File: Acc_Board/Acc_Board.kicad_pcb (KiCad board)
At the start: 2 copper layers, 139.7 x 88.9 mm, 85 parts, among them J1 AIRs Power, J10 Conn_01x02_Pin, J12 776087-1, J2 IsoSPI, J3 IMD BAT, J4 HV Power, J5 HVIL, J6 IMD, J7 Current Sensor, J8 Fans, J9 Shutdown IL, K1 Relay_SPST-NO, K2 Latching Relay, Q1 STS6NF20V, Q2 STS6NF20V, Q3 STS6NF20V, Q4 STS6NF20V, U1 ISO1050DUB, U10 DK1A1B-12V, U11 NSL-32, U12 LTC6820, U13 NAND, U15 MCP6004, U16 NSL-32, U17 NSL-32, U2 NUCLEO-L432KC, U3 LM555N, U4 PQDE6W-Q110-S5-H-D, U5 R-78B5.0-2.0, U6 NSL-32, U7 DK1A1B-12V, U8 LM7809_TO220, U9 NSL-32

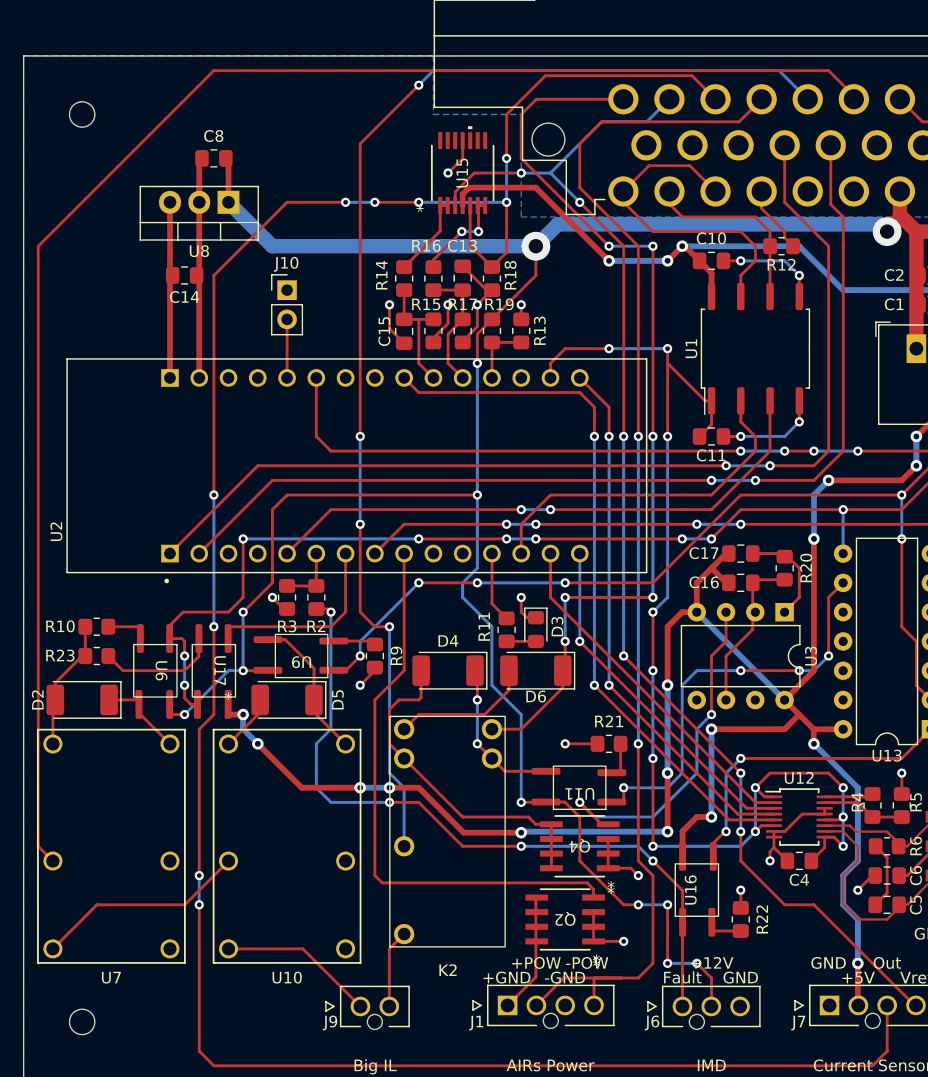
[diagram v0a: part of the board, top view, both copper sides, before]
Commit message: acc board fixed opto footprints
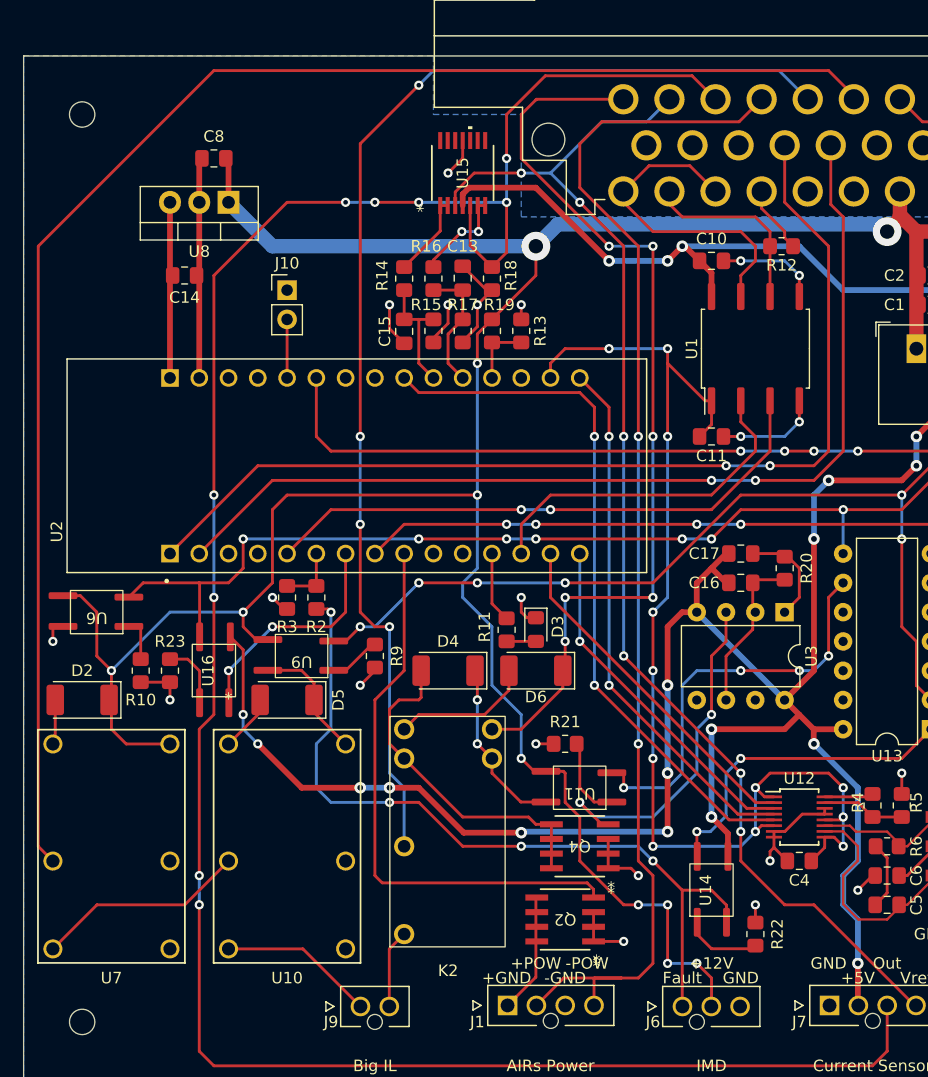
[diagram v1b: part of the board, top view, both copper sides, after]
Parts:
- removed U17: NSL-32, 1FS_2_Global_Footprint_Library:OptoCoupler 6-SOP
- added U14: TLP3122AE, 1FS_2_Global_Footprint_Library:OptoCoupler 6-SOP, F.Cu at (72.4, 85.1)
- U11, U16, U6, U9: value NSL-32 -> TLP3122AE
- moved U16 46.0 mm to (29.2, 66.0)
- moved U6 7.18 mm to (19.1, 61.0), turned to 180 degrees
- moved R23 6.48 mm to (25.4, 66.0), turned to -90 degrees
- moved R10 5.39 mm to (22.9, 66.0), turned to -90 degrees
- moved R21 3.81 mm to (59.7, 72.4)
- moved R22 1.80 mm to (76.2, 88.9)
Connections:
- D2 pad 1: Net-(D2-K) -> +12V
- R10 pad 1: Net-(U6-K) -> Net-(R10-Pad1)
- R21 pad 1: Net-(U11-K) -> Net-(R21-Pad1)
- R22 pad 1: Net-(U16-K) -> Net-(R22-Pad1)
- R23 pad 1: Net-(U17-K) -> Net-(R23-Pad1)
- R9 pad 2: Net-(U9-K) -> Net-(R9-Pad2)
- U11 pad 1: Net-(U11-A) -> Net-(R21-Pad1)
- U11 pad 3: Net-(D4-K) -> Net-(U11-Pad3)
- U13 pad 9: Net-(U11-A) -> Net-(U11-Pad3)
- U16 pad 1: /IMD_FAULT -> Net-(R23-Pad1)
- U16 pad 3: /IMD_FAULT_5V -> /BMS_FAULT
- U6 pad 1: /BMS_FAULT_5V -> Net-(R10-Pad1)
- U6 pad 3: Net-(D2-K) -> /BMS_FAULT_5V
- U7 pad 8: Net-(D2-K) -> +12V
- U9 pad 1: /IMD_FAULT_5V -> Net-(R9-Pad2)
- U9 pad 3: Net-(D5-K) -> /IMD_FAULT_5V
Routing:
- net Net-(U11-A): track 36.0 -> 0.00 mm, vias 4 -> 0
- net Net-(U11-Pad3): track 0.00 -> 35.1 mm, vias 0 -> 4
- net +12V: track 289.0 -> 310.5 mm, vias 12 -> 11
- net Net-(U17-K): track 10.4 -> 0.00 mm
- net Net-(D2-K): track 7.75 -> 0.00 mm
- net Net-(R21-Pad1): track 0.00 -> 7.22 mm
- net Net-(R22-Pad1): track 0.00 -> 6.73 mm
- net /IMD_FAULT: track 62.7 -> 68.5 mm
- net Net-(R23-Pad1): track 0.00 -> 5.75 mm
- net Net-(R9-Pad2): track 0.00 -> 4.49 mm
- net +5V: track 244.3 -> 248.1 mm
- net Net-(U9-K): track 3.69 -> 0.00 mm
- net /BMS_FAULT: track 16.8 -> 20.1 mm, vias 0 -> 2
- net Net-(U11-K): track 3.13 -> 0.00 mm
- net Net-(U16-K): track 3.13 -> 0.00 mm
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
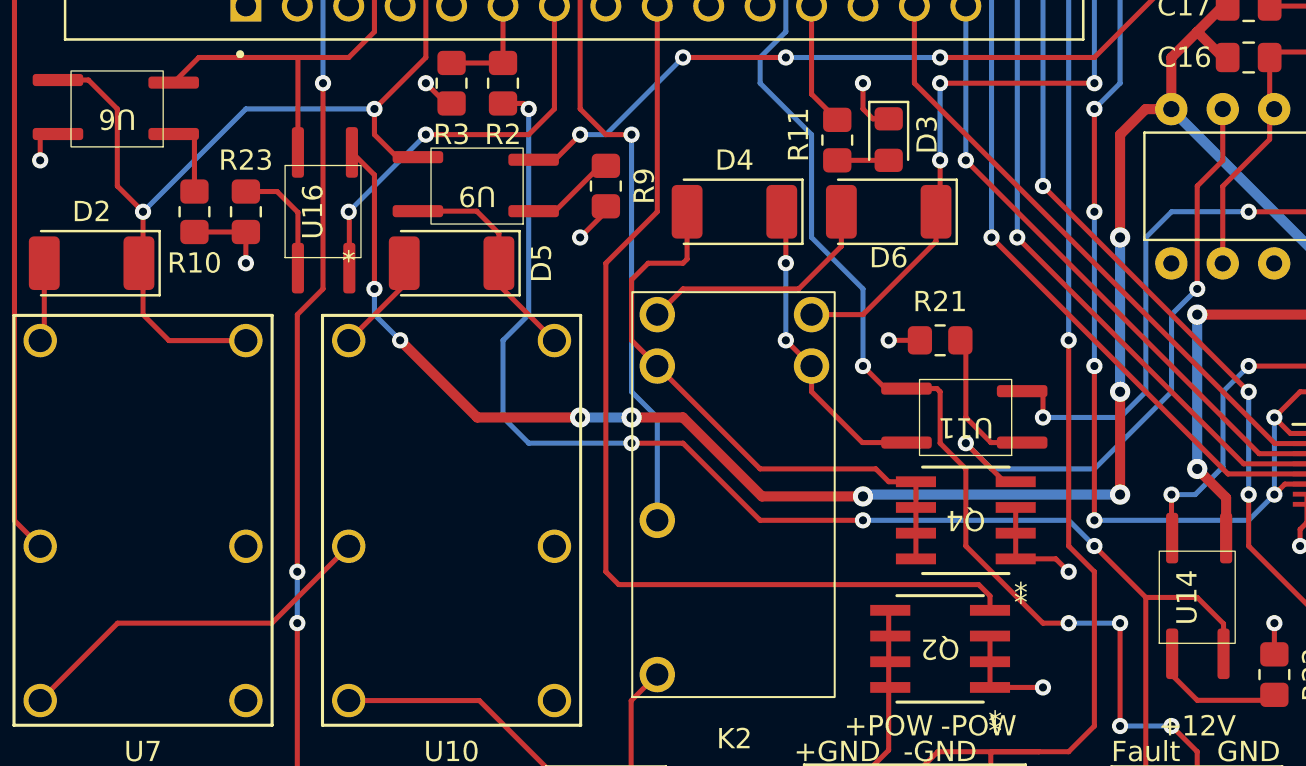
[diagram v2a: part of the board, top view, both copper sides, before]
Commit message: fixed opto silkscreen on acc board
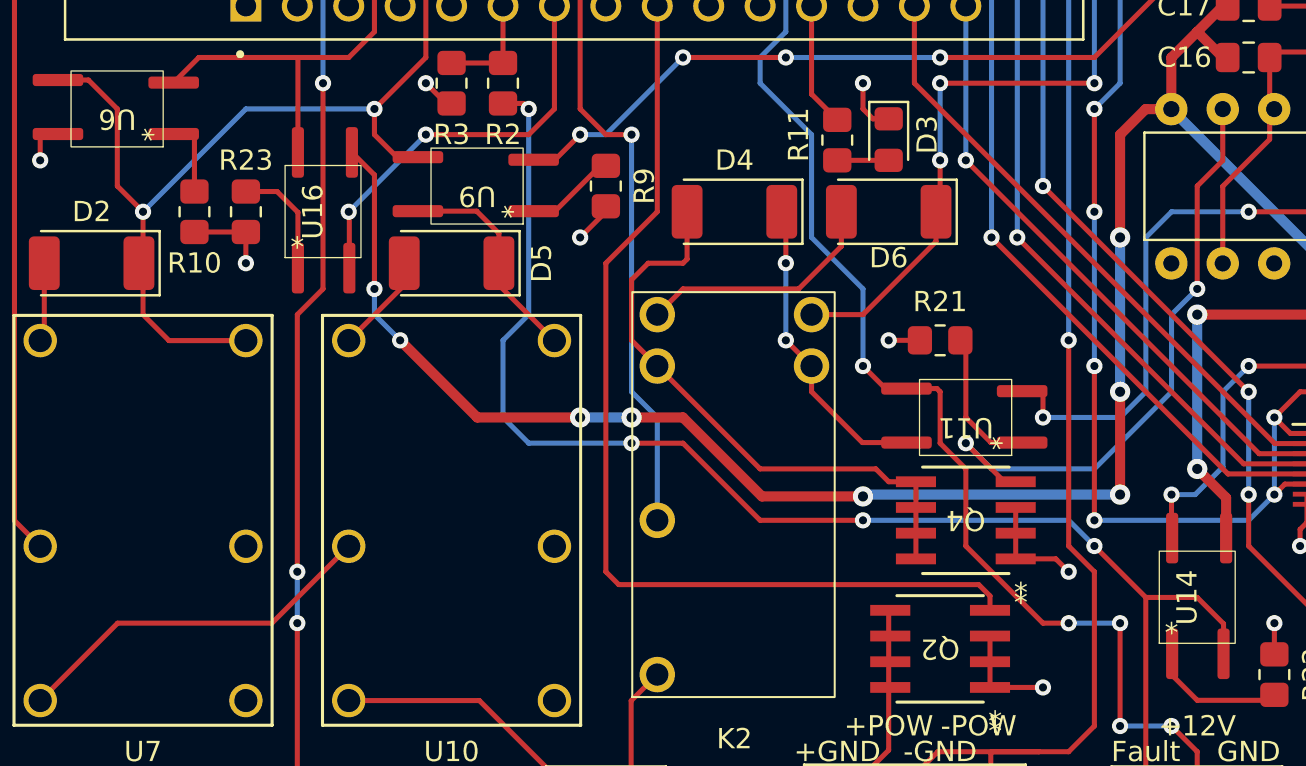
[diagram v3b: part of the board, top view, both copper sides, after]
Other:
- board text added: "*"
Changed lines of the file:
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@@
         (effects (font (size 1 1) (thickness 0.15)))
     )
-    (fp_text user "*" (at 0 -3.928533 unlocked) (layer "F.SilkS")
-        (effects (font (size 1 1) (thickness 0.15)))
-    )
     (fp_text user "*" (at 0 -1.693333 unlocked) (layer "F.Fab")
         (effects (font (size 1 1) (thickness 0.15)))
@@
     (effects (font (size 1 1) (thickness 0.15)) (justify right mirror))
   )
+  (gr_text "*" (at 71.12 86.36 180) (layer "F.SilkS")
+    (effects (font (size 1 1) (thickness 0.15)))
+  )
   (gr_text "L" (at 142.24 35.56 90) (layer "F.SilkS")
     (effects (font (size 1 1) (thickness 0.15)))
@@
     (effects (font (size 1 1) (thickness 0.15)))
   )
+  (gr_text "*" (at 38.1 66.04 -90) (layer "F.SilkS")
+    (effects (font (size 1 1) (thickness 0.15)))
+  )
   (gr_text "N" (at 143.51 80.01 90) (layer "F.SilkS")
     (effects (font (size 1 1) (thickness 0.15)))
@@
     (effects (font (size 1 1) (thickness 0.15)))
   )
+  (gr_text "*" (at 27.94 67.31 180) (layer "F.SilkS")
+    (effects (font (size 1 1) (thickness 0.15)))
+  )
   (gr_text "TS-" (at 109.855 92.71) (layer "F.SilkS")
     (effects (font (size 1 1) (thickness 0.15)))
@@
     (effects (font (size 1 1) (thickness 0.15)))
   )
+  (gr_text "*" (at 62.23 77.47 -90) (layer "F.SilkS")
+    (effects (font (size 1 1) (thickness 0.15)))
+  )
   (gr_text "TS" (at 105.41 88.9) (layer "F.SilkS")
     (effects (font (size 1 1) (thickness 0.15)) (justify left))
@@
     (effects (font (size 1 1) (thickness 0.15)))
   )
+  (gr_text "*" (at 20.32 62.23 -90) (layer "F.SilkS")
+    (effects (font (size 1 1) (thickness 0.15)))
+  )

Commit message: Updade acc board version #
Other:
- board text added: "FS-2 Acc Board Formula Slug V 1.5"
- board text removed: "FS-2 Acc Board Formula Slug V 1.4"
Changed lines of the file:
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@@
   (title_block
     (title "Accumulator Board")
-    (date "2024-02-26")
-    (rev "1.4")
+    (date "2024-03-01")
+    (rev "1.5")
     (company "Formula Slug")
   )
@@
     (effects (font (size 1 1) (thickness 0.15)))
   )
-  (gr_text "FS-2 Acc Board\nFormula Slug\nV 1.4" (at 124.46 33.02) (layer "F.SilkS")
+  (gr_text "FS-2 Acc Board\nFormula Slug\nV 1.5" (at 124.46 33.02) (layer "F.SilkS")
     (effects (font (size 1 1) (thickness 0.15)) (justify left))
   )

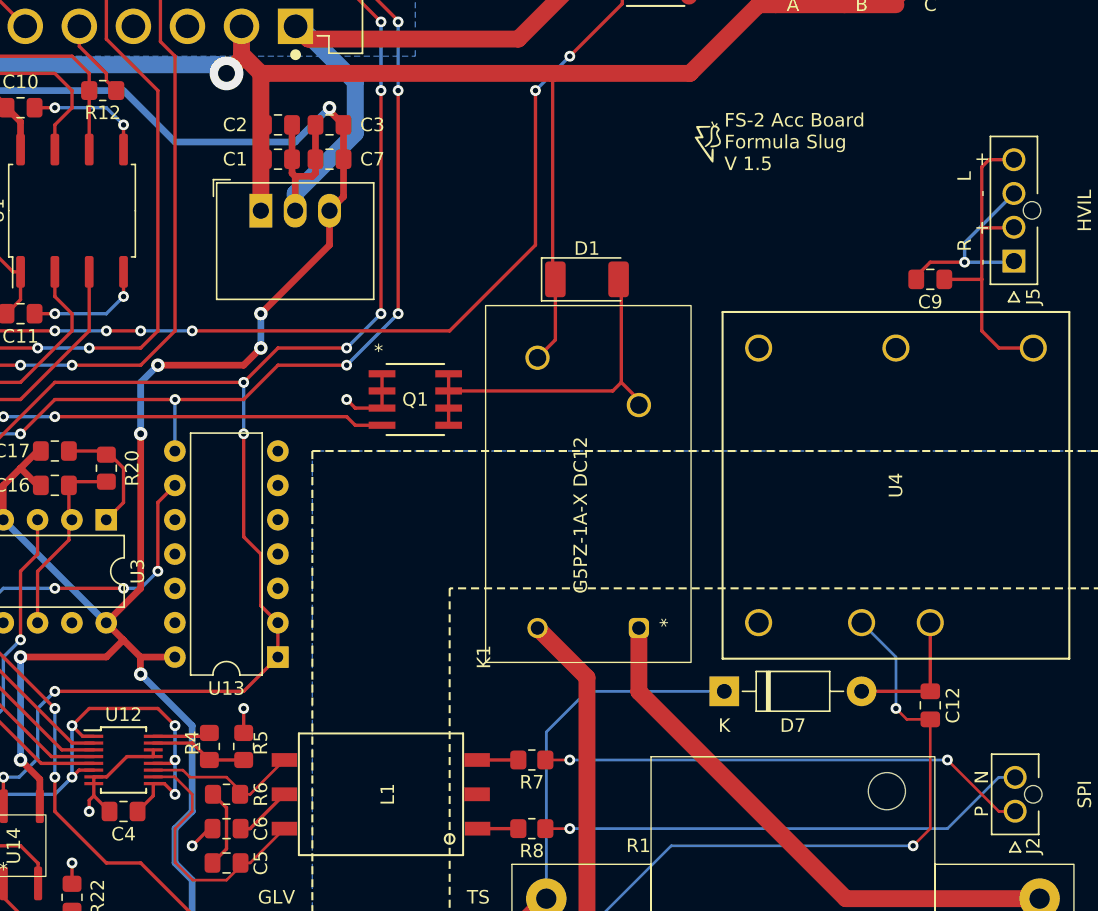
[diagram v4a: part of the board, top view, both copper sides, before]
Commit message: Fixed crossover traces for SPI on acc board
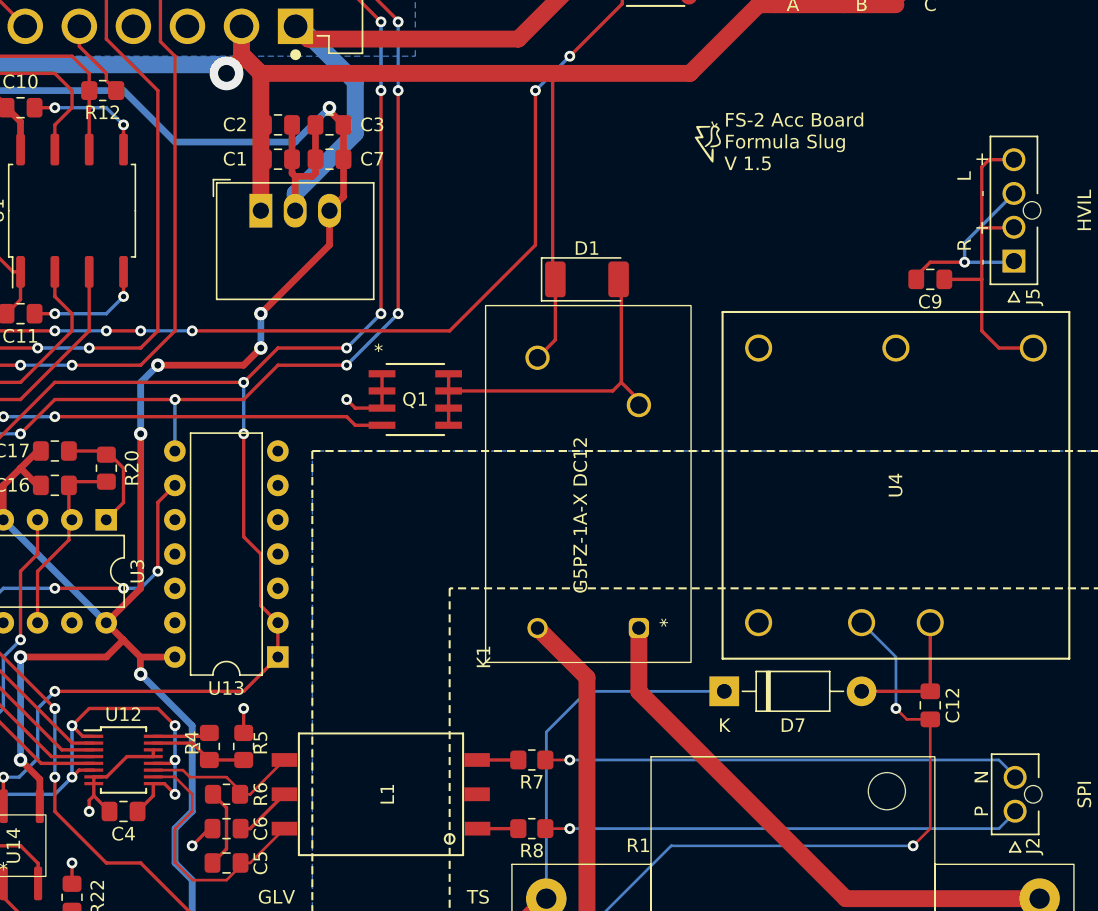
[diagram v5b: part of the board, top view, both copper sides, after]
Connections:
- J2 pad 1: /Iso SPI/extIsoSPI_P -> /Iso SPI/extIsoSPI_N
- J2 pad 2: /Iso SPI/extIsoSPI_N -> /Iso SPI/extIsoSPI_P
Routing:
- net /Iso SPI/extIsoSPI_P: track 36.3 -> 35.3 mm, vias 2 -> 1
- net /Iso SPI/extIsoSPI_N: track 36.3 -> 35.3 mm
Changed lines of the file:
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@@
       (drillshape 0)
       (scaleselection 1)
-      (outputdirectory "C:/Users/coles/Downloads/")
+      (outputdirectory "../Gerbers/")
     )
   )
@@
     (pad "" np_thru_hole circle (at 1.25 1.34 90) (size 1.3 1.3) (drill 1.3) (layers "*.Cu" "*.Mask"))
     (pad "1" thru_hole circle (at 0 0 90) (size 1.7 1.7) (drill 1.2) (layers "*.Cu")
-      (net 19 "/Iso SPI/extIsoSPI_P") (pinfunction "1") (pintype "passive"))
+      (net 20 "/Iso SPI/extIsoSPI_N") (pinfunction "1") (pintype "passive"))
     (pad "2" thru_hole circle (at 2.5 0 90) (size 1.7 1.7) (drill 1.2) (layers "*.Cu")
-      (net 20 "/Iso SPI/extIsoSPI_N") (pinfunction "2") (pintype "passive"))
+      (net 19 "/Iso SPI/extIsoSPI_P") (pinfunction "2") (pintype "passive"))
     (model "${FS_2_SCHEMATICS}/3D Models/1053091202.step"
       (offset (xyz 1.25 4.85 0))
@@
     (fp_line (start 1 0.625) (end -1 0.625)
       (stroke (width 0.1) (type solid)) (layer "F.Fab"))
-    (pad "1" smd roundrect (at -1 0 180) (size 1.2 1.4) (layers "F.Cu" "F.Paste" "F.Mask") (roundrect_rratio 0.208333)
+    (pad "1" smd roundrect (at -1 0 180) (size 1.2 1.4) (layers "F.Cu" "F.Paste" "F.Mask") (roundrect_rratio 0.2083333333)
       (net 26 "/CAN_L_RES") (pintype "passive"))
-    (pad "2" smd roundrect (at 1 0 180) (size 1.2 1.4) (layers "F.Cu" "F.Paste" "F.Mask") (roundrect_rratio 0.208333)
+    (pad "2" smd roundrect (at 1 0 180) (size 1.2 1.4) (layers "F.Cu" "F.Paste" "F.Mask") (roundrect_rratio 0.2083333333)
       (net 90 "/CAN_L") (pintype "passive"))
     (model "${KICAD6_3DMODEL_DIR}/Resistor_SMD.3dshapes/R_0805_2012Metric.wrl"
@@
   (segment (start 66.04 45.72) (end 66.04 72.39) (width 0.25) (layer "B.Cu") (net 18))
   (segment (start 111.22 78.74) (end 113.03 78.74) (width 0.2) (layer "F.Cu") (net 19))
-  (segment (start 144.78 82.55) (end 145.96 82.55) (width 0.2) (layer "F.Cu") (net 19))
-  (segment (start 145.96 82.55) (end 145.98 82.53) (width 0.2) (layer "F.Cu") (net 19))
-  (segment (start 140.97 78.74) (end 144.78 82.55) (width 0.2) (layer "F.Cu") (net 19))
-  (via (at 140.97 78.74) (size 0.8) (drill 0.4) (layers "F.Cu" "B.Cu") (net 19))
   (via (at 113.03 78.74) (size 0.8) (drill 0.4) (layers "F.Cu" "B.Cu") (net 19))
-  (segment (start 140.97 78.74) (end 113.03 78.74) (width 0.2) (layer "B.Cu") (net 19))
+  (segment (start 144.78 78.74) (end 145.98 79.94) (width 0.2) (layer "B.Cu") (net 19))
+  (segment (start 113.03 78.74) (end 144.78 78.74) (width 0.2) (layer "B.Cu") (net 19))
+  (segment (start 145.98 79.94) (end 145.98 80.03) (width 0.2) (layer "B.Cu") (net 19))
   (segment (start 113.03 83.82) (end 111.22 83.82) (width 0.2) (layer "F.Cu") (net 20))
   (via (at 113.03 83.82) (size 0.8) (drill 0.4) (layers "F.Cu" "B.Cu") (net 20))
-  (segment (start 140.97 83.82) (end 113.03 83.82) (width 0.2) (layer "B.Cu") (net 20))
-  (segment (start 145.98 80.03) (end 144.76 80.03) (width 0.2) (layer "B.Cu") (net 20))
-  (segment (start 144.76 80.03) (end 140.97 83.82) (width 0.2) (layer "B.Cu") (net 20))
+  (segment (start 145.98 82.62) (end 145.98 82.53) (width 0.2) (layer "B.Cu") (net 20))
+  (segment (start 144.78 83.82) (end 145.98 82.62) (width 0.2) (layer "B.Cu") (net 20))
+  (segment (start 113.03 83.82) (end 144.78 83.82) (width 0.2) (layer "B.Cu") (net 20))
   (segment (start 143.30575 100.33) (end 120.77425 100.33) (width 0.2) (layer "F.Cu") (net 21))
   (segment (start 145.89 97.74575) (end 143.30575 100.33) (width 0.2) (layer "F.Cu") (net 21))
